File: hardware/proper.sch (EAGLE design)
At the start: 42 parts, among them IC1 MEGA8-PU, IC3 MAX232, Q1 16MHz, T1 2N3904, T2 2N3904

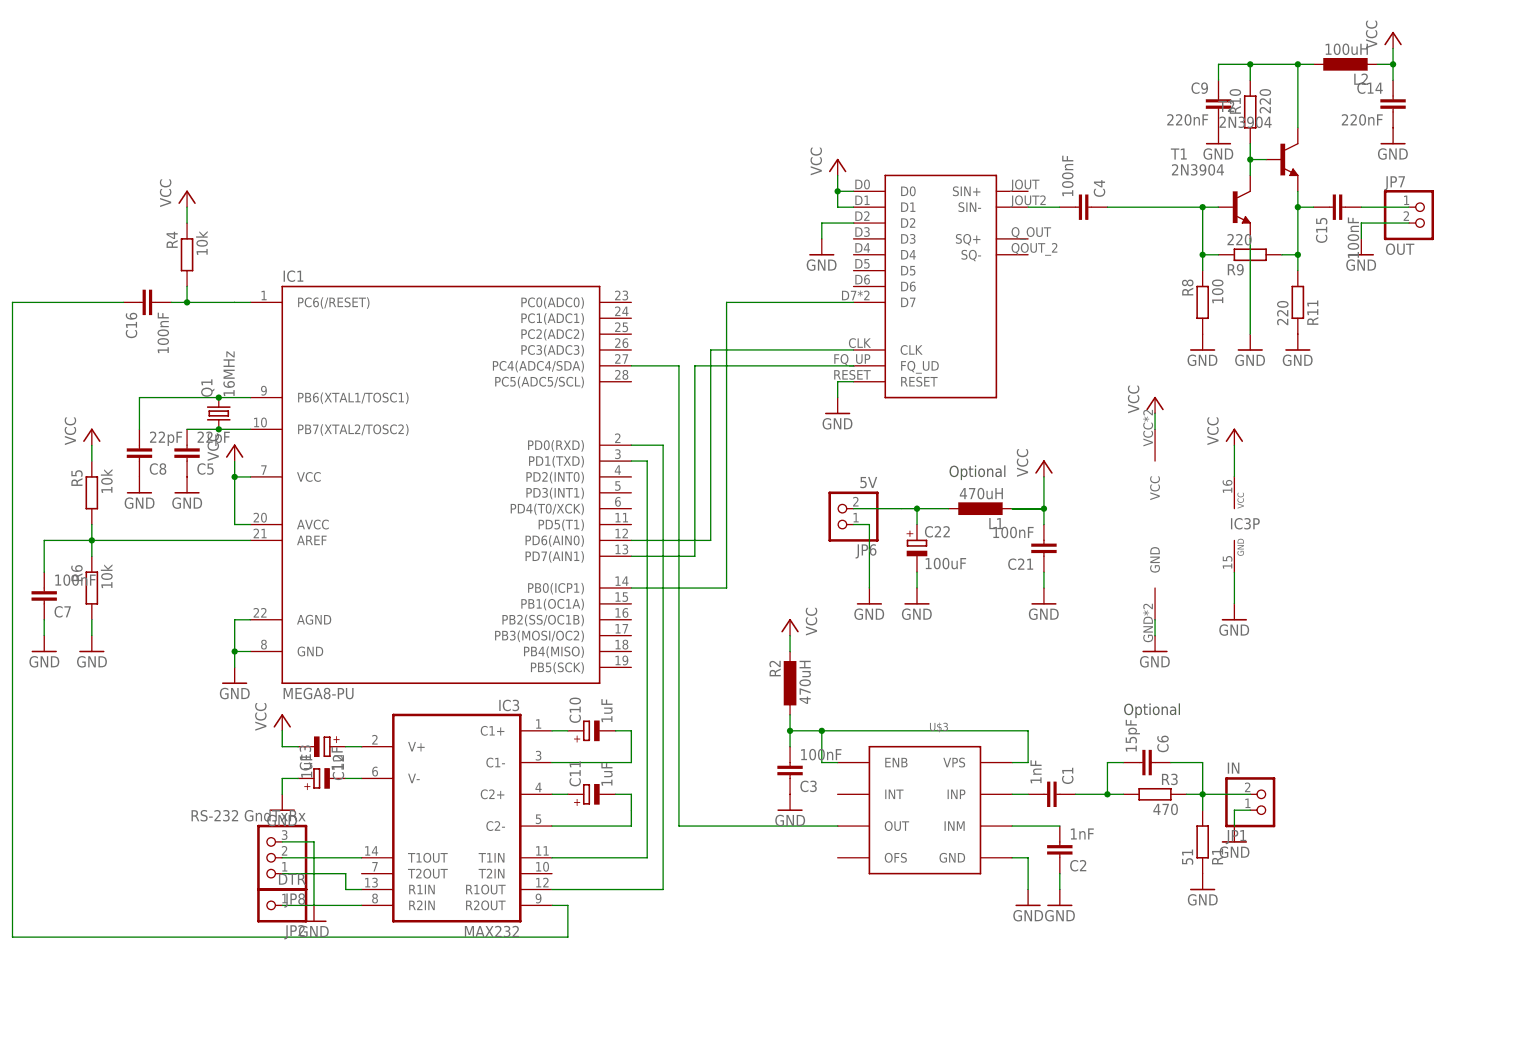
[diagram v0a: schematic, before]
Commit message: Fixed minors, added win build.
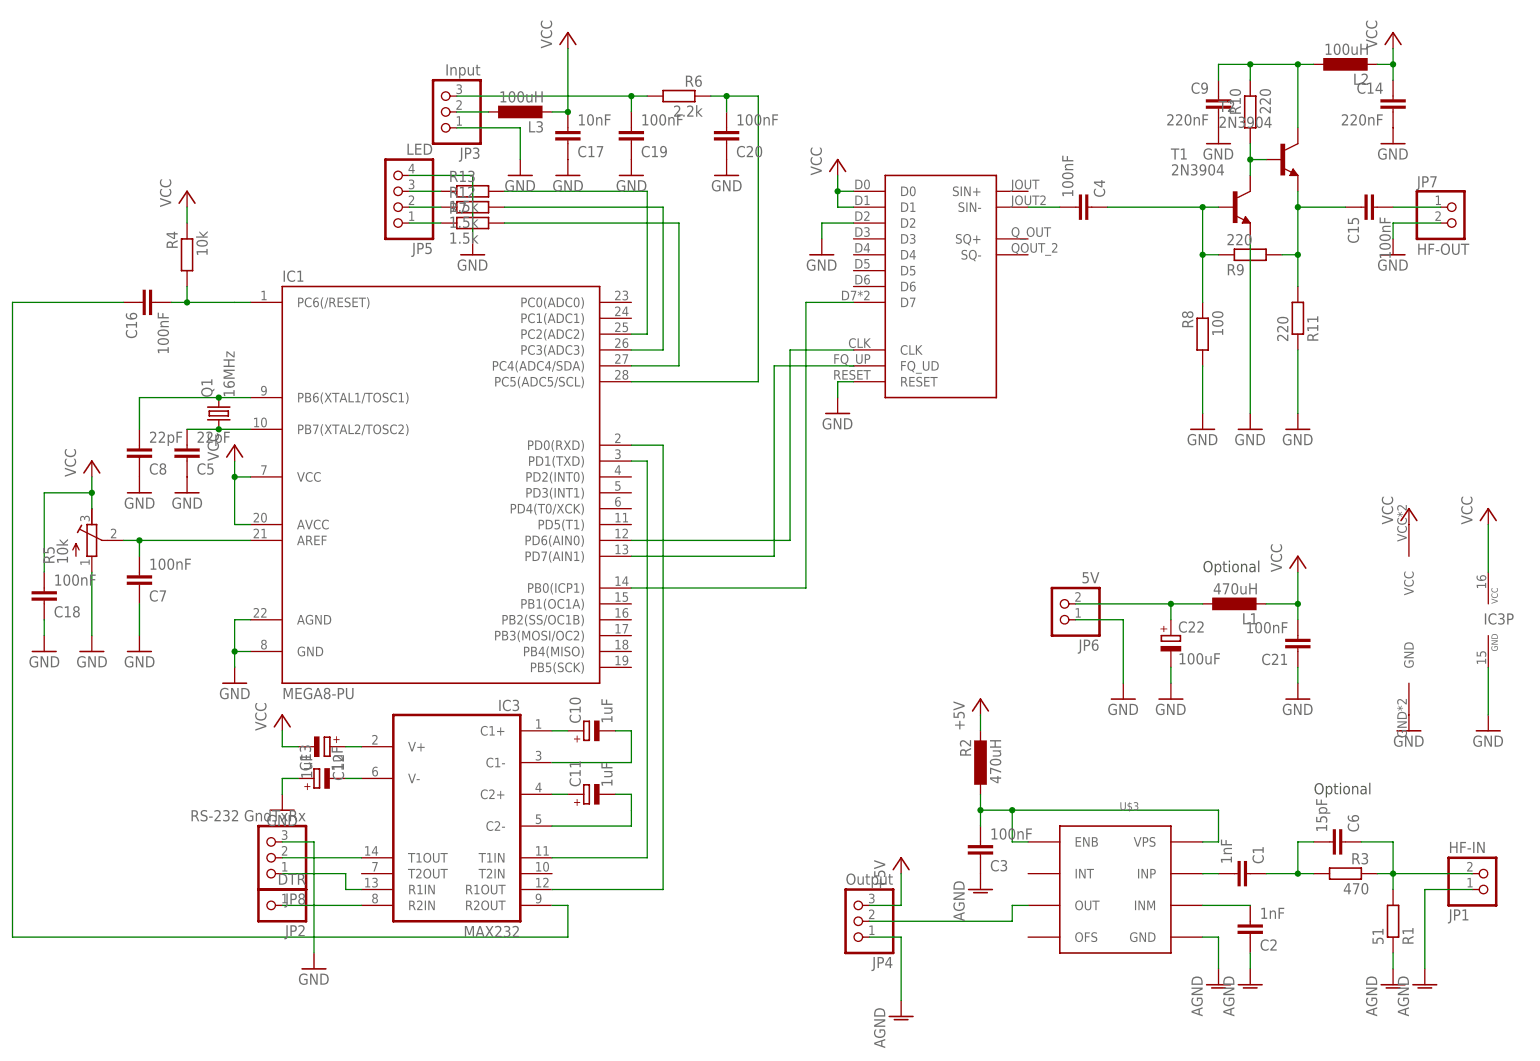
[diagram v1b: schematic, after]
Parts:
- added C17: 10nF, rcl:C-EU025-025X050
- added C18: 100nF, rcl:C-EU050-025X075
- added C19, C20: 100nF, rcl:C-EU025-025X050
- added JP3: Input, pinhead:PINHD-1X3
- added JP4: Output, pinhead:PINHD-1X3
- added JP5: LED, pinhead:PINHD-1X4
- added L3: 100uH, rcl:L-EU0207/2V
- added R12, R13, R7: 1.5k, rcl:R-EU_0204/5
- C1: device rcl:C-EU050-025X075 -> rcl:C-EU025-025X050
- C10: device rcl:CPOL-EUE2.5-6 -> rcl:CPOL-EUE2.5-5
- C13: device rcl:CPOL-EUE5-5 -> rcl:CPOL-EUE2.5-5
- C14, C6: device rcl:C-EU025-025X050 -> rcl:C-EU050-025X075
- JP1: value IN -> HF-IN
- JP7: value OUT -> HF-OUT
- L2: device rcl:L-EU0204/7 -> rcl:L-EU0207/12
- R3: device rcl:R-EU_0204/2V -> rcl:R-EU_0204/5
- R5: device rcl:R-EU_0204/2V -> rcl:R-TRIMM64W
- R6: value 10k -> 2.2k; device rcl:R-EU_0204/5 -> rcl:R-EU_0204/2V
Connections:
- new net +5V: JP4.3, R2.2
- new net N$14: C20.2, IC1.PC5(ADC5/SCL), R6.1
- new net N$28: C7.2, IC1.AREF, R5.S
- new net N$30: JP5.1, R7.1
- new net N$31: JP5.2, R12.1
- new net N$32: JP5.3, R13.1
- new net N$33: C2.1, C3.1, JP1.1, JP4.1, R1.1, U$3.GND
- new net N$35: IC1.PC4(ADC4/SDA), R7.2
- new net N$36: IC1.PC3(ADC3), R12.2
- new net N$37: IC1.PC2(ADC2), R13.2
- new net N$42: C19.2, JP3.3, R6.2
- net GND: now also C17.1, C18.1, C19.1, C20.1, JP3.1, JP5.4, R5.A; no longer C2.1, C3.1, JP1.1, R1.1, R6.2, U$3.GND
- net N$29: now also JP3.2, L3.1; no longer C7.2, IC1.AREF, R5.2, R6.1
- net N$9: now also JP4.2; no longer IC1.PC4(ADC4/SDA)
- net VCC: now also C17.2, C18.2, L3.2, R5.E; no longer R2.2, R5.1
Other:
- moved on the sheet: C1, C15, C2, C21, C22, C3, C6, C7, IC3P, JP1, JP6, JP7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
